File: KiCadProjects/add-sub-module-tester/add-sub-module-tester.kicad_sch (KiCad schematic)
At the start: 27 parts, among them J1 2x4_Connector, J2 1x2_Connector, J3 12V In, SW1 PWR_SW, U1 Toggle_Switch_3PIN, U2 Toggle_Switch_3PIN, U3 Toggle_Switch_3PIN, U4 Toggle_Switch_3PIN, U5 AP6503

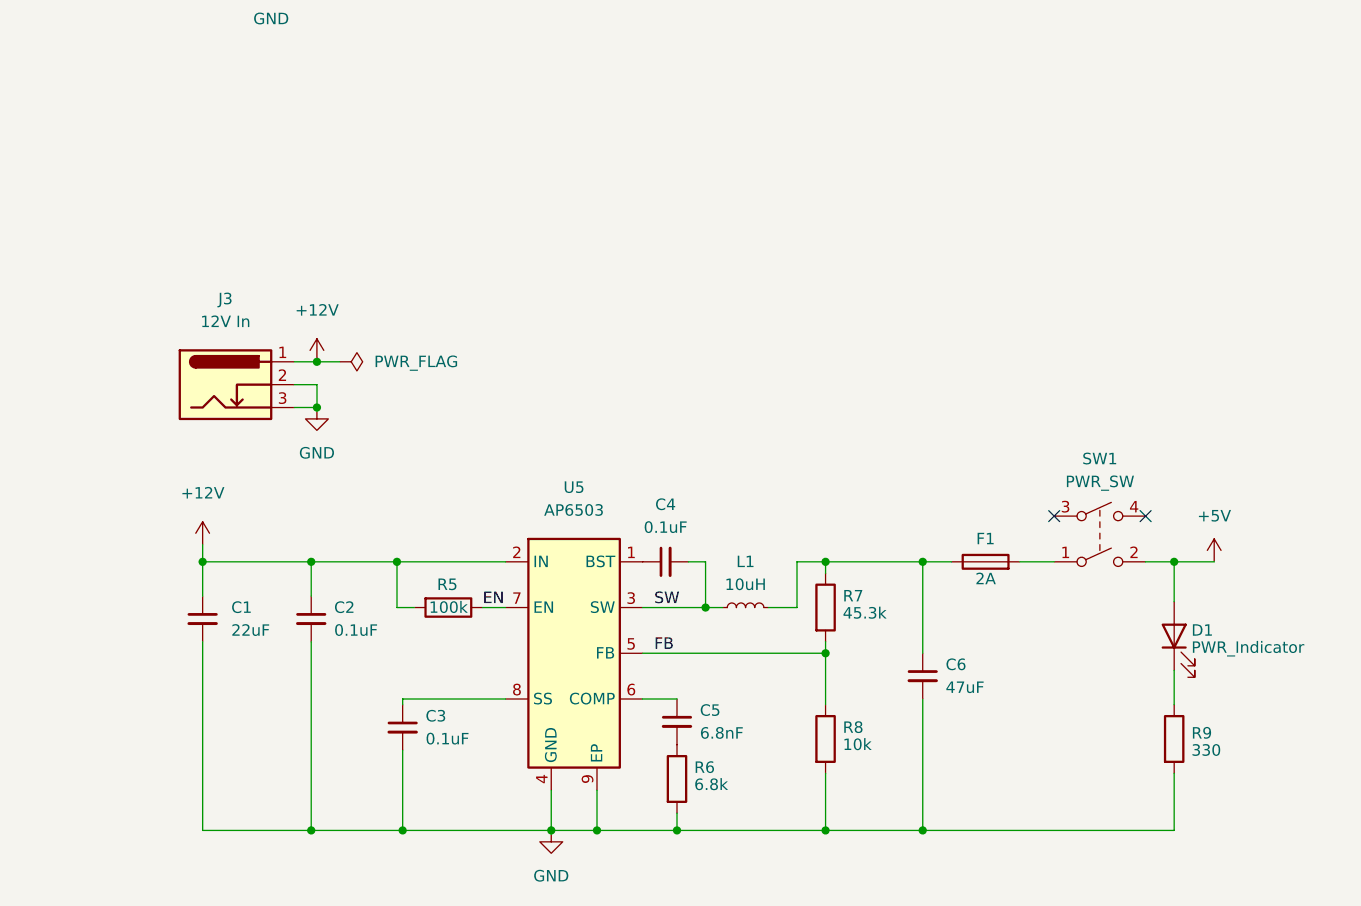
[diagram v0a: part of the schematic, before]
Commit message: finished tester design
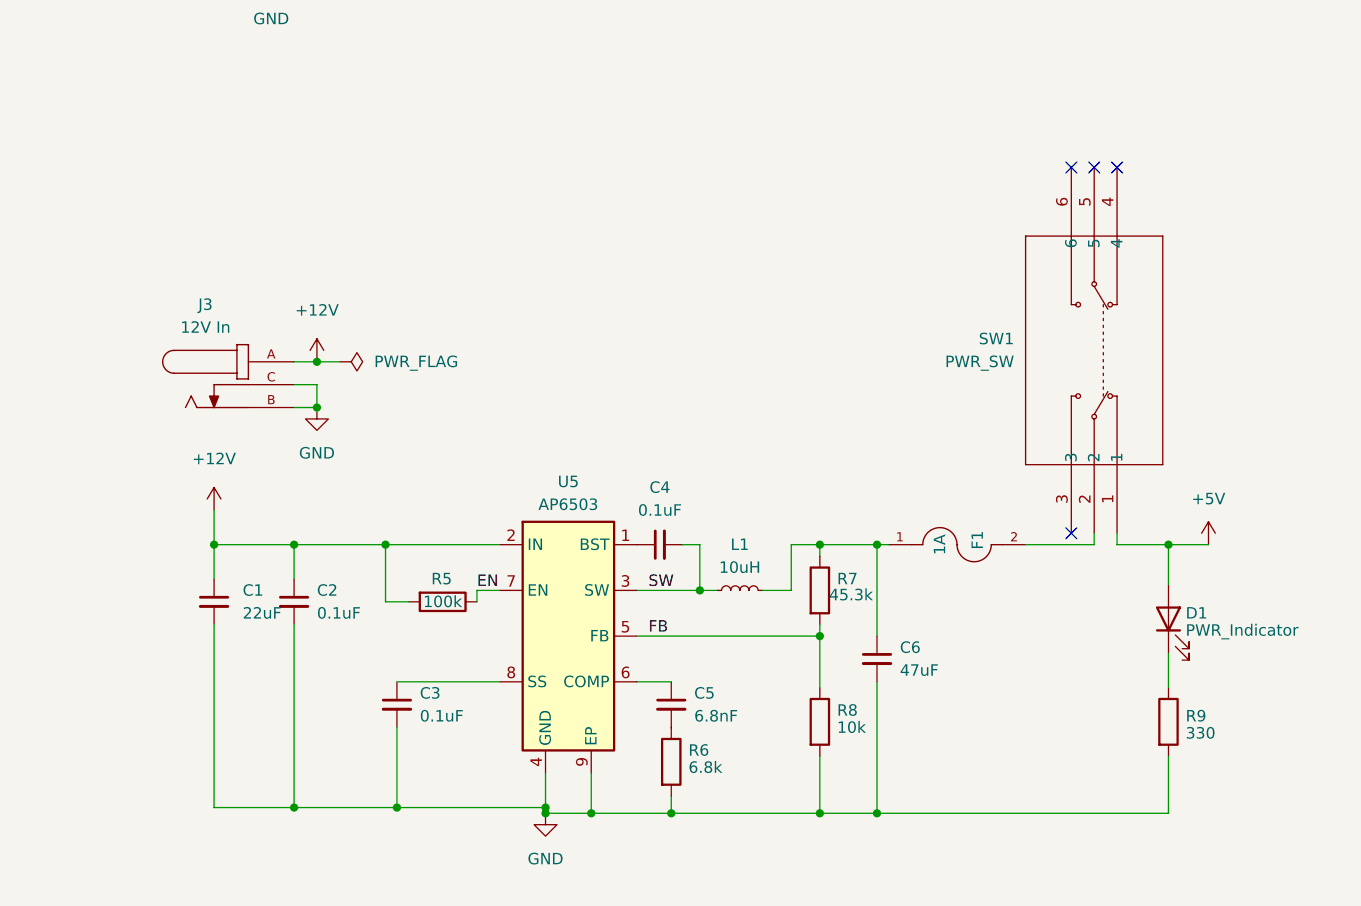
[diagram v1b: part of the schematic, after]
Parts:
- C1: footprint Capacitor_SMD:CP_Elec_4x4.5 -> 0_add_sub_module_tester:CP_Elec_4x5.4; LCSC (none) -> C3356; Link (none) -> https://jlcpcb.com/partdetail/HonorElec-RVT1C220M0405/C3356; Part No (none) -> C3356
- C2, C3, C4: footprint Capacitor_SMD:C_0603_1608Metric_Pad1.08x0.95mm_HandSolder -> 0_add_sub_module_tester:C_0603_1608Metric; LCSC (none) -> C1590; Link (none) -> https://jlcpcb.com/partdetail/1942-CL10B104KA8NNNC/C1590; Part No (none) -> C1590
- C5: footprint Capacitor_SMD:C_0603_1608Metric_Pad1.08x0.95mm_HandSolder -> 0_add_sub_module_tester:C_0603_1608Metric; LCSC (none) -> C81355; Link (none) -> https://jlcpcb.com/partdetail/82506-0603B682K101NT/C81355; Part No (none) -> C81355
- C6: footprint Capacitor_SMD:CP_Elec_6.3x7.7 -> 0_add_sub_module_tester:CP_Elec_6.3x7.7; LCSC (none) -> C3349; Link (none) -> https://jlcpcb.com/partdetail/HonorElec-RVT1H470M0607/C3349; Part No (none) -> C3349
- D1: footprint LED_THT:LED_D5.0mm -> 0_add_sub_module_tester:LED_0805_2012Metric; LCSC (none) -> C2297; Link (none) -> https://jlcpcb.com/partdetail/Hubei_KentoElec-KT0805G/C2297; Part No (none) -> C2297
- F1: value 2A -> 1A; footprint Fuse:Fuseholder_Cylinder-5x20mm_Bulgin_FX0457_Horizontal_Closed -> 0_add_sub_module_tester:Fuse_Holder; symbol Device:Fuse -> 0_add_sub_module_tester:Fuse_Holder; LCSC (none) -> 4628; Link (none) -> https://www.digikey.com/en/products/detail/keystone-electro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; MANUFACTURER (none) -> Keystone; MAXIMUM_PACKAGE_HEIGHT (none) -> 11.99mm; Part No (none) -> 36-4628-ND; SNAPEDA_PN (none) -> 4628; STANDARD (none) -> Manufacturer Recommendation
- J3: footprint Connector_BarrelJack:BarrelJack_Horizontal -> 0_add_sub_module_tester:Jack_Connector; symbol Connector:Barrel_Jack_Switch_Pin3Ring -> 0_add_sub_module_tester:Jack_Connector; LCSC (none) -> 54-00167; Link (none) -> https://www.digikey.com/en/products/detail/tensility-intern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; MANUFACTURER (none) -> TENSILITY; MAXIMUM_PACKAGE_HEIGHT (none) -> 11.2mm; PARTREV (none) -> A; Part No (none) -> 839-54-00167-ND; SNAPEDA_PN (none) -> 54-00166; STANDARD (none) -> Manufacturer Recommendations
- L1: footprint Inductor_SMD:L_Coilcraft_LPS5030 -> 0_add_sub_module_tester:IND-SMD_L4.5-W4.0; LCSC (none) -> C2929419; Link (none) -> https://jlcpcb.com/partdetail/ShouHan-CY4310UH/C2929419; Part No (none) -> C2929419
- R5: footprint Resistor_SMD:R_0603_1608Metric_Pad0.98x0.95mm_HandSolder -> 0_add_sub_module_tester:R_0603_1608Metric; LCSC (none) -> C15458; Link (none) -> https://jlcpcb.com/partdetail/16137-0603WAJ0104T5E/C15458; Part No (none) -> C15458
- R6: footprint Resistor_SMD:R_0603_1608Metric_Pad0.98x0.95mm_HandSolder -> 0_add_sub_module_tester:R_0603_1608Metric; LCSC (none) -> C26004; Link (none) -> https://jlcpcb.com/partdetail/26747-0603WAJ0682T5E/C26004; Part No (none) -> C26004
- R7: footprint Resistor_SMD:R_0603_1608Metric_Pad0.98x0.95mm_HandSolder -> 0_add_sub_module_tester:R_0603_1608Metric; LCSC (none) -> C101054; Link (none) -> https://jlcpcb.com/partdetail/LizElec-CR0603FA4532G/C101054; Part No (none) -> C101054
- R8: footprint Resistor_SMD:R_0603_1608Metric_Pad0.98x0.95mm_HandSolder -> 0_add_sub_module_tester:R_0603_1608Metric; LCSC (none) -> C15401; Link (none) -> https://jlcpcb.com/partdetail/16079-0603WAJ0103T5E/C15401; Part No (none) -> C15401
- R9: footprint Resistor_SMD:R_0603_1608Metric_Pad0.98x0.95mm_HandSolder -> 0_add_sub_module_tester:R_0603_1608Metric; LCSC (none) -> C22104; Link (none) -> https://jlcpcb.com/partdetail/22829-RS03K331JT/C22104; Part No (none) -> C22104
- SW1: footprint Imported:SW_PB400EEQR1BLK -> 0_add_sub_module_tester:Slide_Switch_Angled; symbol Switch:SW_DPST -> 0_add_sub_module_tester:Slide_Switch_Angled; LCSC (none) -> MFS201N-16-Z; Link (none) -> https://www.digikey.com/en/products/detail/nidec-components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; Part No (none) -> 563-1558-ND
- U5: footprint Package_SO:Diodes_SO-8EP -> 0_add_sub_module_tester:AP6503; symbol Regulator_Switching:AP6503 -> 0_add_sub_module_tester:AP6503; LCSC (none) -> C51811; Link (none) -> https://jlcpcb.com/partdetail/DiodesIncorporated-AP6503SP13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; Part No (none) -> C51811
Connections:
- net +12V: now also J3.A; no longer J3.1
- net +5V: now also SW1.1; no longer SW1.2
- net GND: now also J3.B, J3.C; no longer J3.2, J3.3
- net at F1.2: now also SW1.2; no longer SW1.1
- no-connect marks 6 -> 8
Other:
- moved on the sheet: C5, C6, D1, L1, R6, R7, R8, R9, U5

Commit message: still working on tester
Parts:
- removed U2, U3, U4: Toggle_Switch_3PIN, 0_add_sub_module_tester:Toggle_Switch_3PIN, symbol 0_add_sub_module_tester:Toggle_Switch_3PIN
- added U2, U3, U4: Toggle_Switch_3PIN, easyeda2kicad:SW-TH_MT-0-103-A101-M200-RS, symbol 0_add_sub_module_tester:MT-0-103-A101-M200-RS+PJ
- SW1: footprint 0_add_sub_module_tester:Slide_Switch_Angled -> easyeda2kicad:SW-TH_SK12D07VG5; symbol 0_add_sub_module_tester:Slide_Switch_Angled -> easyeda2kicad:SK12D07VG5; LCSC MFS201N-16-Z -> C431548; LCSC Part (none) -> C431548; Link https://www.digikey.com/en/products/detail/nidec-components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 -> https://www.lcsc.com/product-detail/Slide-Switches_SHOU-HAN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; Part No 563-1558-ND -> C431548
- U1: footprint 0_add_sub_module_tester:Toggle_Switch_3PIN -> easyeda2kicad:SW-TH_MT-0-103-A101-M200-RS; symbol 0_add_sub_module_tester:Toggle_Switch_3PIN -> 0_add_sub_module_tester:MT-0-103-A101-M200-RS+PJ; LCSC ANT11SF1CQE -> C1788493; LCSC Part (none) -> C1788493; Link https://www.digikey.com/en/products/detail/cit-relay-and-sw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 -> https://www.lcsc.com/product-detail/Toggle-Switches_YUEN-FU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; Part No 2449-ANT11SF1CQE-ND -> C1788493
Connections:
- net +5V: now also U2.1, U3.1, U4.1; no longer SW1.1
- net ADD/SUB: now also U4.2
- net CARRY: now also U3.2
- net KA: now also U2.2
- net at SW1.2: no longer F1.2
- net at R4.1: now also U3.3
- net at R3.1: now also U4.3
- net at R2.1: now also U2.3
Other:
- moved on the sheet: R1, R2, R3, R4

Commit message: made some slight adjustments
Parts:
- removed F1: 1A, 0_add_sub_module_tester:Fuse_Holder, symbol 0_add_sub_module_tester:Fuse_Holder
- removed U5: AP6503, 0_add_sub_module_tester:AP6503, symbol 0_add_sub_module_tester:AP6503
- added U5: AP6503, Package_SO:Diodes_SO-8EP, symbol Regulator_Switching:AP6503
- C1: footprint 0_add_sub_module_tester:CP_Elec_4x5.4 -> Capacitor_SMD:CP_Elec_4x4.5; LCSC C3356 -> (none); Link https://jlcpcb.com/partdetail/HonorElec-RVT1C220M0405/C3356 -> (none); Part No C3356 -> (none)
- C2, C3, C4: footprint 0_add_sub_module_tester:C_0603_1608Metric -> Capacitor_SMD:C_0603_1608Metric_Pad1.08x0.95mm_HandSolder; LCSC C1590 -> (none); Link https://jlcpcb.com/partdetail/1942-CL10B104KA8NNNC/C1590 -> (none); Part No C1590 -> (none)
- C5: footprint 0_add_sub_module_tester:C_0603_1608Metric -> Capacitor_SMD:C_0603_1608Metric_Pad1.08x0.95mm_HandSolder; LCSC C81355 -> (none); Link https://jlcpcb.com/partdetail/82506-0603B682K101NT/C81355 -> (none); Part No C81355 -> (none)
- C6: footprint 0_add_sub_module_tester:CP_Elec_6.3x7.7 -> Capacitor_SMD:CP_Elec_6.3x7.7; LCSC C3349 -> (none); Link https://jlcpcb.com/partdetail/HonorElec-RVT1H470M0607/C3349 -> (none); Part No C3349 -> (none)
- J3: footprint 0_add_sub_module_tester:Jack_Connector -> Connector_BarrelJack:BarrelJack_Horizontal; LCSC 54-00167 -> C136744; Link https://www.digikey.com/en/products/detail/tensility-intern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 -> https://www.lcsc.com/product-detail/DC-Power-Connectors_Kor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; Part No 839-54-00167-ND -> C136744
- L1: footprint 0_add_sub_module_tester:IND-SMD_L4.5-W4.0 -> Inductor_SMD:L_Coilcraft_LPS5030; LCSC C2929419 -> (none); Link https://jlcpcb.com/partdetail/ShouHan-CY4310UH/C2929419 -> (none); Part No C2929419 -> (none)
- R5: footprint 0_add_sub_module_tester:R_0603_1608Metric -> Resistor_SMD:R_0603_1608Metric_Pad0.98x0.95mm_HandSolder; LCSC C15458 -> (none); Link https://jlcpcb.com/partdetail/16137-0603WAJ0104T5E/C15458 -> (none); Part No C15458 -> (none)
- R6: footprint 0_add_sub_module_tester:R_0603_1608Metric -> Resistor_SMD:R_0603_1608Metric_Pad0.98x0.95mm_HandSolder; LCSC C26004 -> (none); Link https://jlcpcb.com/partdetail/26747-0603WAJ0682T5E/C26004 -> (none); Part No C26004 -> (none)
- R7: footprint 0_add_sub_module_tester:R_0603_1608Metric -> Resistor_SMD:R_0603_1608Metric_Pad0.98x0.95mm_HandSolder; LCSC C101054 -> (none); Link https://jlcpcb.com/partdetail/LizElec-CR0603FA4532G/C101054 -> (none); Part No C101054 -> (none)
- R8: footprint 0_add_sub_module_tester:R_0603_1608Metric -> Resistor_SMD:R_0603_1608Metric_Pad0.98x0.95mm_HandSolder; LCSC C15401 -> (none); Link https://jlcpcb.com/partdetail/16079-0603WAJ0103T5E/C15401 -> (none); Part No C15401 -> (none)
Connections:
- net +12V: now also U5.2 (IN)
- net +5V: now also SW1.2
- net EN: now also U5.7 (EN)
- net FB: now also U5.5 (FB)
- net GND: now also SW1.1, SW1.4, SW1.5, U5.4 (GND), U5.9 (EP)
- net SW: now also U5.3 (SW)
- net at SW1.3: now also C6.1, L1.2, R7.1
- net at C4.1: now also U5.1 (BST)
- net at C5.1: now also U5.6 (COMP)
- net at C3.1: now also U5.8 (SS)
- no-connect marks 8 -> 4
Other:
- moved on the sheet: SW1

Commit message: initial updates after meeting
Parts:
- J1: footprint 0_add_sub_module_tester:2x4_Connector -> Connector_PinSocket_2.54mm:PinSocket_2x04_P2.54mm_Vertical; LCSC PPTC042LFBN-RC -> C2977588; Link https://www.digikey.com/en/products/detail/sullins-connecto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 -> https://www.lcsc.com/product-detail/Female-Headers_ZHOURI-2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; Part No S7072-ND -> C2977588
- J2: footprint 0_add_sub_module_tester:1x2_Connector -> Connector_PinSocket_2.54mm:PinSocket_1x02_P2.54mm_Vertical; LCSC PPTC021LFBN-RC -> C7499322; Link https://www.digikey.com/en/products/detail/sullins-connecto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 -> https://www.lcsc.com/product-detail/Female-Headers_Megastar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; Part No S7000-ND -> C7499322
- J3: symbol 0_add_sub_module_tester:Jack_Connector -> Connector:Barrel_Jack_Switch
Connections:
- net +12V: now also J3.1; no longer J3.A
- net GND: now also J3.2, J3.3, SW1.3; no longer J3.B, J3.C, SW1.1
- net at C6.1, L1.2, R7.1: now also SW1.1; no longer SW1.3

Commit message: final updates for Revision A
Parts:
- removed J1: 2x4_Connector, Connector_PinSocket_2.54mm:PinSocket_2x04_P2.54mm_Vertical, symbol 0_add_sub_module_tester:2x4_Connector
- removed J2: 1x2_Connector, Connector_PinSocket_2.54mm:PinSocket_1x02_P2.54mm_Vertical, symbol 0_add_sub_module_tester:1x2_Connector
- added H1, H2, H3, H4, H5, H6: MountingHole_Pad, MountingHole:MountingHole_3.2mm_M3_DIN965_Pad, symbol Mechanical:MountingHole_Pad
- added J1, J2: Conn_01x04_Socket, Connector_PinSocket_2.54mm:PinSocket_1x04_P2.54mm_Vertical, symbol Connector:Conn_01x04_Socket
- added J4: Conn_01x02_Socket, Connector_PinSocket_2.54mm:PinSocket_1x02_P2.54mm_Vertical, symbol Connector:Conn_01x02_Socket
- C1: footprint Capacitor_SMD:CP_Elec_4x4.5 -> Capacitor_SMD:CP_Elec_5x5.4; LCSC (none) -> C239256; Link (none) -> https://www.lcsc.com/product-detail/Aluminum-Electrolytic-C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; Part No (none) -> C239256
- C2, C3, C4: LCSC (none) -> C14663; Link (none) -> https://www.lcsc.com/product-detail/Multilayer-Ceramic-Capa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; Part No (none) -> C14663
- C5: LCSC (none) -> C1631; Link (none) -> https://www.lcsc.com/product-detail/Multilayer-Ceramic-Capa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; Part No (none) -> C1631
- C6: LCSC (none) -> C72523; Link (none) -> https://www.lcsc.com/product-detail/Aluminum-Electrolytic-C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; Part No (none) -> C72523
- D1: footprint 0_add_sub_module_tester:LED_0805_2012Metric -> LED_SMD:LED_0805_2012Metric_Pad1.15x1.40mm_HandSolder; Link https://jlcpcb.com/partdetail/Hubei_KentoElec-KT0805G/C2297 -> https://www.lcsc.com/product-detail/LED-Indication-Discrete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
- L1: LCSC (none) -> C20417074; Link (none) -> https://www.lcsc.com/product-detail/Power-Inductors_Coilcra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; Part No (none) -> C20417074
- R1, R2, R3, R4: value R -> 330; footprint 0_add_sub_module_tester:R_Axial_DIN0207_L6.3mm_D2.5mm_P7.62mm_Horizontal -> Resistor_THT:R_Axial_DIN0207_L6.3mm_D2.5mm_P7.62mm_Horizontal; LCSC (none) -> C2935230; Link (none) -> https://www.lcsc.com/product-detail/Through-Hole-Resistors_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; Part No (none) -> C2935230
- R5: LCSC (none) -> C14675; Link (none) -> https://www.lcsc.com/product-detail/Chip-Resistor-Surface-M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; Part No (none) -> C14675
- R6: LCSC (none) -> C114632; Link (none) -> https://www.lcsc.com/product-detail/Chip-Resistor-Surface-M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; Part No (none) -> C114632
- R7: LCSC (none) -> C23058; Link (none) -> https://www.lcsc.com/product-detail/Chip-Resistor-Surface-M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; Part No (none) -> C23058
- R8: LCSC (none) -> C2930027; Link (none) -> https://www.lcsc.com/product-detail/Chip-Resistor-Surface-M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; Part No (none) -> C2930027
- R9: footprint 0_add_sub_module_tester:R_0603_1608Metric -> Resistor_SMD:R_0603_1608Metric_Pad0.98x0.95mm_HandSolder; Link https://jlcpcb.com/partdetail/22829-RS03K331JT/C22104 -> https://www.lcsc.com/product-detail/Chip-Resistor-Surface-M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
- U5: LCSC (none) -> C51811; Link (none) -> https://www.lcsc.com/product-detail/DC-DC-Converters_Diodes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; Part No (none) -> C51811
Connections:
- net +5V: now also J1.1 (Pin_1)
- net ADD/SUB: now also J2.3 (Pin_3)
- net CA: now also J2.1 (Pin_1)
- net CARRY: now also J2.4 (Pin_4)
- net GND: now also H1.1, H2.1, H3.1, H4.1, H5.1, H6.1, J1.4 (Pin_4)
- net KA: now also J2.2 (Pin_2)

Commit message: FINAL final changes for Rev. A
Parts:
- D1: footprint LED_SMD:LED_0805_2012Metric_Pad1.15x1.40mm_HandSolder -> LED_SMD:LED_0603_1608Metric_Pad1.05x0.95mm_HandSolder; LCSC C2297 -> C125098; Link https://www.lcsc.com/product-detail/LED-Indication-Discrete_Hubei-KENTO-Elec-KT-0805G_C2297.html -> https://www.lcsc.com/product-detail/LED-Indication-Discrete_Lite-On-LTST-C191KGKT_C125098.html; Part No C2297 -> C125098
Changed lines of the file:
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@@
 			)
 		)
-		(property "Footprint" "LED_SMD:LED_0805_2012Metric_Pad1.15x1.40mm_HandSolder"
+		(property "Footprint" "LED_SMD:LED_0603_1608Metric_Pad1.05x0.95mm_HandSolder"
 			(at 234.315 130.175 0)
 			(effects
@@
 			)
 		)
-		(property "Part No" "C2297"
+		(property "Part No" "C125098"
 			(at 234.315 130.175 0)
 			(effects
@@
 			)
 		)
-		(property "Link" "https://www.lcsc.com/product-detail/LED-Indication-Discrete_Hubei-KENTO-Elec-KT-0805G_C2297.html"
+		(property "Link" "https://www.lcsc.com/product-detail/LED-Indication-Discrete_Lite-On-LTST-C191KGKT_C125098.html"
 			(at 234.315 130.175 0)
 			(effects
@@
 			)
 		)
-		(property "LCSC" "C2297"
+		(property "LCSC" "C125098"
 			(at 234.315 130.175 0)
 			(effects

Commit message: Rev. A v.1.2
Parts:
- J3: LCSC C136744 -> C136744; Part No C136744 -> C136744
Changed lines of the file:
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@@
 			)
 		)
-		(property "Part No" "  C136744"
+		(property "Part No" "C136744"
 			(at 128.27 104.14 0)
 			(effects
@@
 			)
 		)
-		(property "LCSC" "  C136744"
+		(property "LCSC" "C136744"
 			(at 128.27 104.14 0)
 			(effects
